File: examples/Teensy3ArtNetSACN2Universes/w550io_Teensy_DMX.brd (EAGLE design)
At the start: 98.7 x 64.8 mm, 33 parts, among them IC1 MAX481CPA, IC2 MAX481CPA

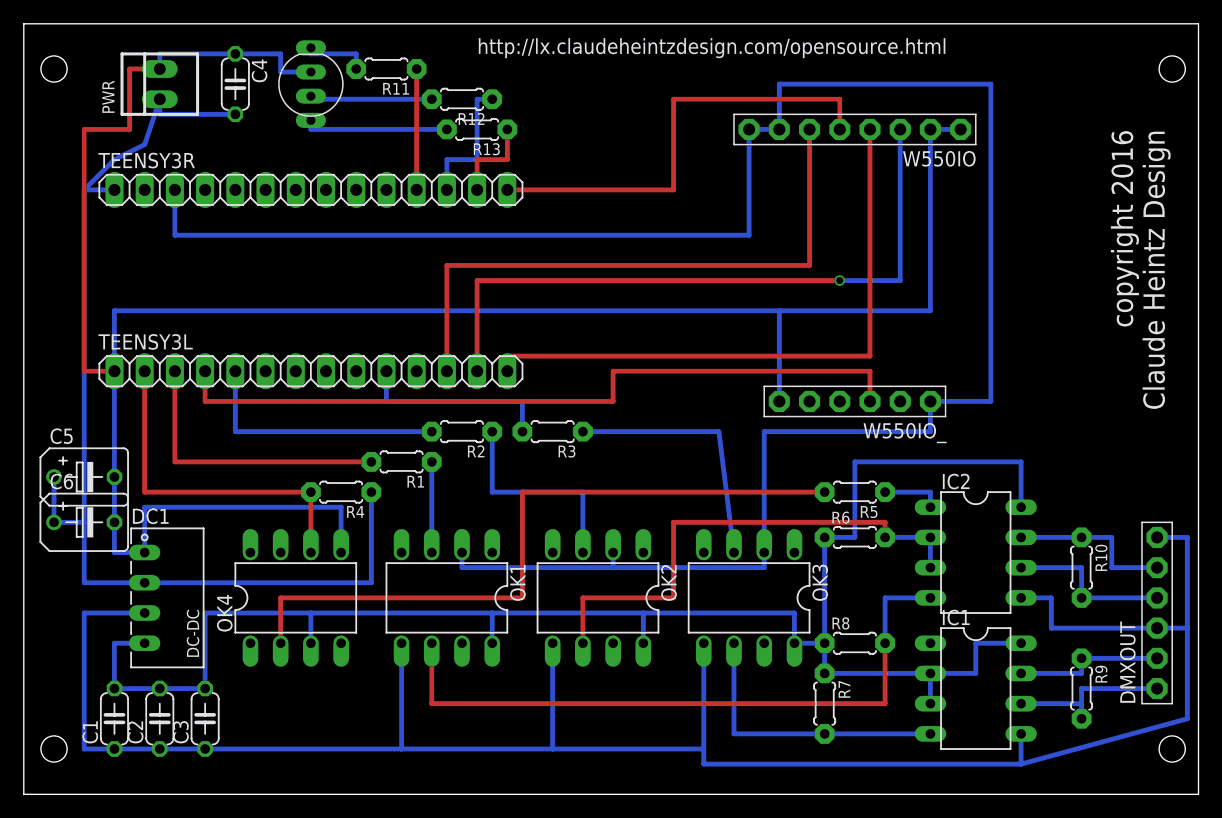
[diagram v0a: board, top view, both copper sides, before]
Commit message: Change Board to output only
Bi-directional design power is unstable.  Previous design is functional
by not populating input and direction optocouplers.
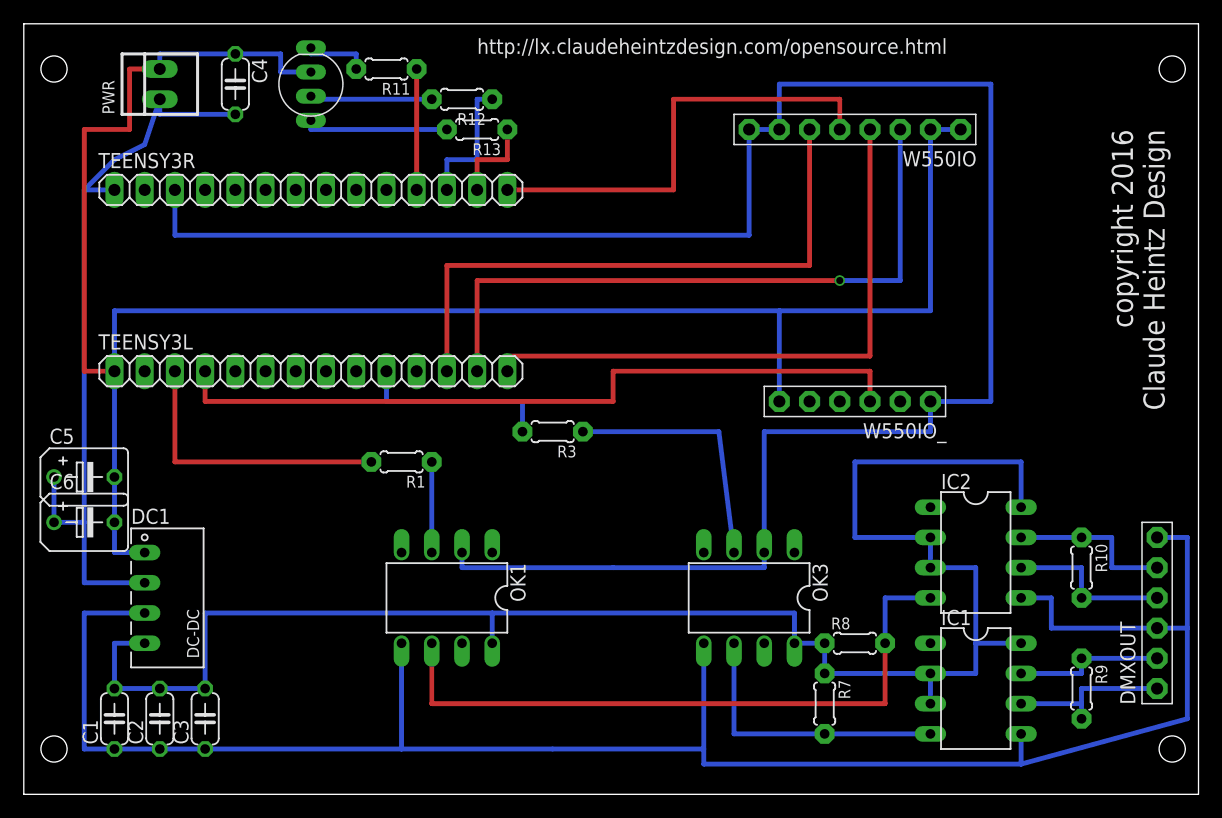
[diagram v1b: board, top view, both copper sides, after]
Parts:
- removed OK2, OK4: 6N137, optocoupler:DIL08
- removed R2: 330, adafruit:0204/5
- removed R4, R6: 10k, adafruit:0204/5
- removed R5: 470, adafruit:0204/5
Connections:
- removed net DX0: R2.2, TEENSY3L.5
- removed net N$1: OK4.2, R5.2
- removed net N$12: IC2.1, R5.1
- removed net N$13: IC2.2, IC2.3, OK2.6, R6.2
- removed net N$6: OK2.3, R2.1
- removed net RX0: OK4.6, R4.2, TEENSY3L.2
- net 3.3V: no longer OK2.2
- net 5VIN: no longer R4.1
- net GND: no longer OK2.5
- net TGND: no longer OK4.5
- net VCC: now also IC2.2, IC2.3; no longer OK2.8, OK4.3, R6.1
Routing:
- net N$1: track 58.4 -> 0.00 mm
- net N$13: track 43.2 -> 0.00 mm
- net RX0: track 29.2 -> 0.00 mm
- net 5VIN: track 91.7 -> 65.1 mm
- net TGND: track 190.8 -> 166.6 mm
- net DX0: track 21.6 -> 0.00 mm
- net N$6: track 17.8 -> 0.00 mm
- net GND: track 174.5 -> 165.6 mm
- net N$12: track 5.08 -> 0.00 mm
- net VCC: track 142.2 -> 144.8 mm
- net 3.3V: track 172.7 -> 171.5 mm

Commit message: Changed 10k Resistors to 1k
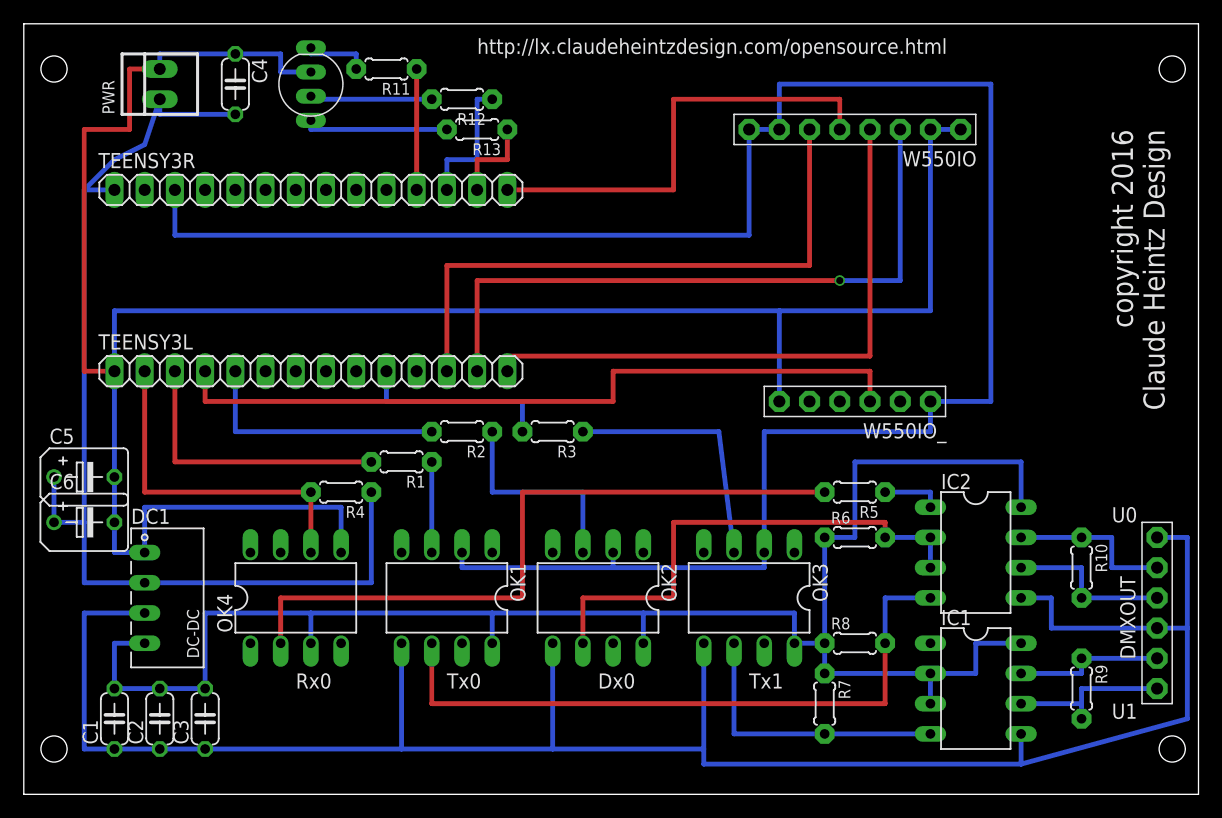
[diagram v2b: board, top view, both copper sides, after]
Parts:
- added OK2, OK4: 6N137, optocoupler:DIL08
- added R2: 330Ω, adafruit:0204/5
- added R4, R6: 1k, adafruit:0204/5
- added R5: 470Ω, adafruit:0204/5
- R1, R11, R12, R13, R3: value 330 -> 330Ω
- R7, R8: value 10k -> 1k
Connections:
- new net DX0: R2.2, TEENSY3L.5
- new net N$1: OK4.2, R5.2
- new net N$12: IC2.1, R5.1
- new net N$13: IC2.2, IC2.3, OK2.6, R6.2
- new net N$6: OK2.3, R2.1
- new net RX0: OK4.6, R4.2, TEENSY3L.2
- net 3.3V: now also OK2.2
- net 5VIN: now also R4.1
- net GND: now also OK2.5
- net TGND: now also OK4.5
- net VCC: now also OK2.8, OK4.3, R6.1; no longer IC2.2, IC2.3
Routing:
- net N$1: track 0.00 -> 58.4 mm
- net N$13: track 0.00 -> 43.2 mm
- net RX0: track 0.00 -> 29.2 mm
- net 5VIN: track 65.1 -> 91.7 mm
- net TGND: track 166.6 -> 190.8 mm
- net DX0: track 0.00 -> 21.6 mm
- net N$6: track 0.00 -> 17.8 mm
- net GND: track 165.6 -> 174.5 mm
- net N$12: track 0.00 -> 5.08 mm
- net VCC: track 144.8 -> 142.2 mm
- net 3.3V: track 171.5 -> 172.7 mm
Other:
- board text added: "Dx0"
- board text added: "Rx0"
- board text added: "Tx0"
- board text added: "Tx1"
- board text added: "U0"
- board text added: "U1"

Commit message: Changed resistors to 3.3k
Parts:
- R4: value 1k -> 10k
- R6, R7, R8: value 1k -> 3.3k
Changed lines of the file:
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@@
 <element name="R2" library="adafruit" package="0204/5" value="330Ω" x="34.29" y="29.21" rot="R180"/>
 <element name="R3" library="adafruit" package="0204/5" value="330Ω" x="41.91" y="29.21" rot="R180"/>
-<element name="R4" library="adafruit" package="0204/5" value="1k" x="24.13" y="24.13" rot="R180"/>
+<element name="R4" library="adafruit" package="0204/5" value="10k" x="24.13" y="24.13" rot="R180"/>
 <element name="IC1" library="maxim" package="DIL08" value="MAX481CPA" x="77.47" y="7.62" rot="R270">
 <attribute name="OC_FARNELL" value="unknown" x="77.47" y="7.62" size="1.778" layer="27" rot="R270" display="off"/>
@@
 </element>
 <element name="R5" library="adafruit" package="0204/5" value="470Ω" x="67.31" y="24.13" rot="R180"/>
-<element name="R6" library="adafruit" package="0204/5" value="1k" x="67.31" y="20.32"/>
-<element name="R7" library="adafruit" package="0204/5" value="1k" x="64.77" y="6.35" rot="R270"/>
-<element name="R8" library="adafruit" package="0204/5" value="1k" x="67.31" y="11.43"/>
+<element name="R6" library="adafruit" package="0204/5" value="3.3k" x="67.31" y="20.32"/>
+<element name="R7" library="adafruit" package="0204/5" value="3.3k" x="64.77" y="6.35" rot="R270"/>
+<element name="R8" library="adafruit" package="0204/5" value="3.3k" x="67.31" y="11.43"/>
 <element name="R9" library="adafruit" package="0204/5" value="120" x="86.36" y="7.62" rot="R270"/>
 <element name="R10" library="adafruit" package="0204/5" value="120" x="86.36" y="17.78" rot="R270"/>

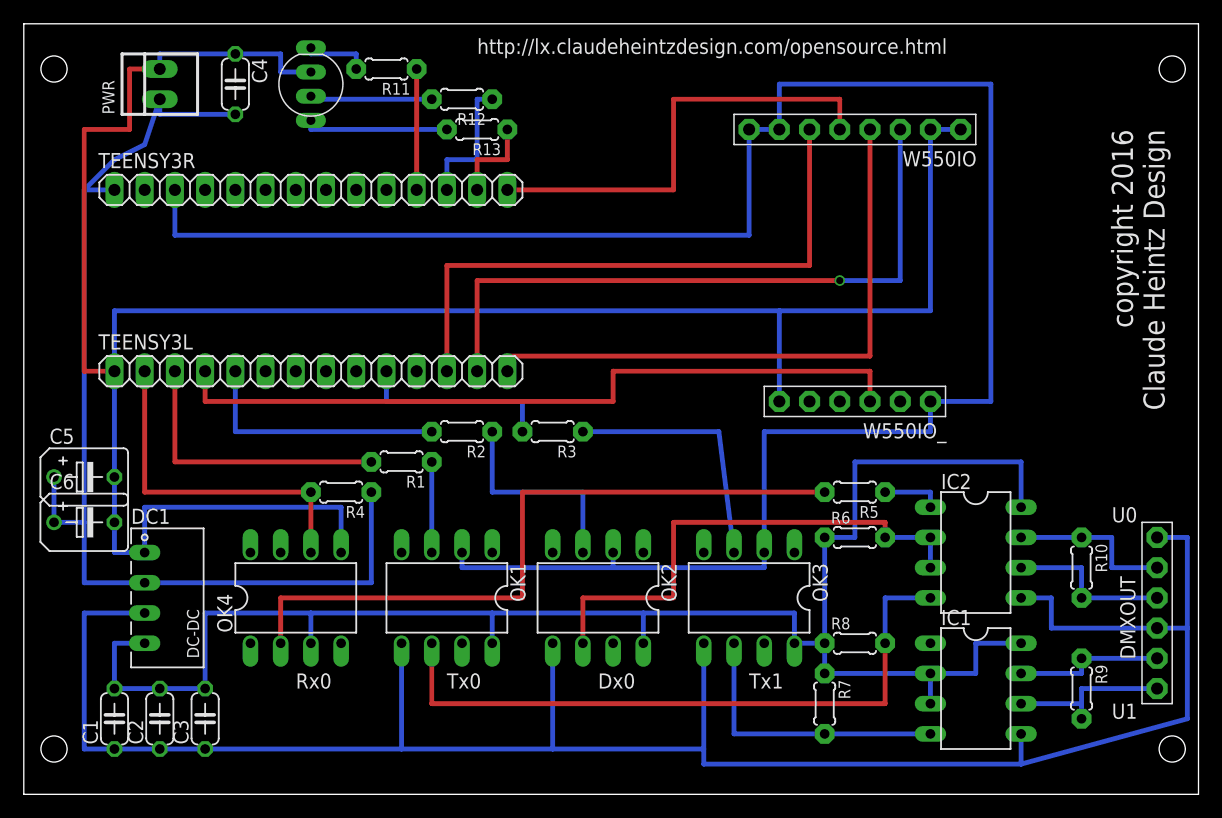
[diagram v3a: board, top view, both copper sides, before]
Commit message: Fix DMX input / example schematic
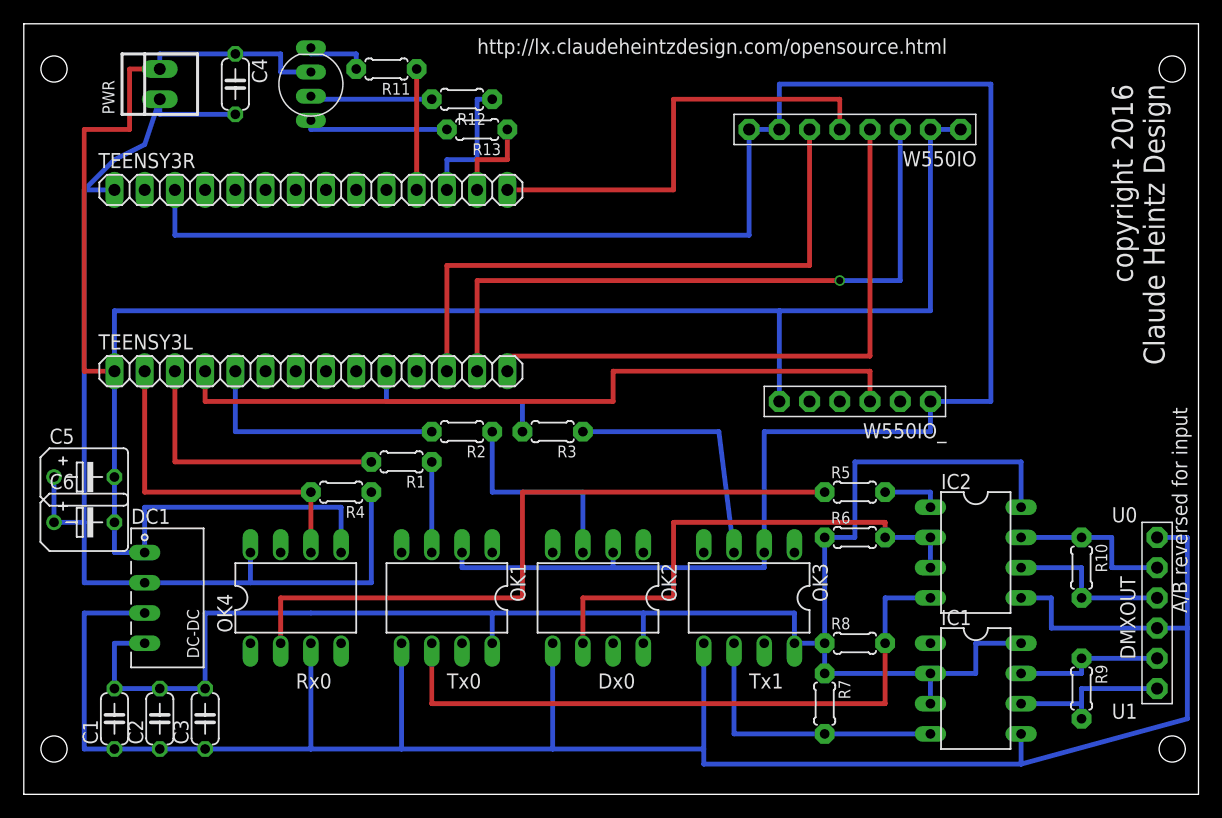
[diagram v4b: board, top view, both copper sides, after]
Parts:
- turned R5 to 0 degrees
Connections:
- net 5VIN: now also OK4.8
- net GND: now also OK4.3
- net N$1: now also R5.1; no longer R5.2
- net N$12: now also R5.2; no longer R5.1
- net VCC: no longer OK4.3
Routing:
- net GND: track 174.5 -> 183.4 mm
- net VCC: track 142.2 -> 139.7 mm
- net 5VIN: track 91.7 -> 94.3 mm
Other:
- board text added: "A/B reversed for input"
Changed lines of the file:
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@@
 <hole x="0" y="59.69" drill="2.2"/>
 <text x="35.56" y="60.96" size="1.27" layer="25" font="vector">http://lx.claudeheintzdesign.com/opensource.html</text>
-<text x="88.9" y="54.61" size="1.778" layer="25" font="vector" rot="R270">copyright 2016
+<text x="88.9" y="58.42" size="1.778" layer="25" font="vector" rot="R270">copyright 2016
 Claude Heintz Design</text>
 <text x="33.02" y="7.62" size="1.27" layer="25">Tx0</text>
@@
 <text x="88.9" y="21.59" size="1.27" layer="25">U0</text>
 <text x="88.9" y="5.08" size="1.27" layer="25">U1</text>
+<text x="95.25" y="13.97" size="1.27" layer="25" rot="R90">A/B reversed for input</text>
 </plain>
 <attributes>
@@
 <attribute name="VALUE" x="90.805" y="7.62" size="1.27" layer="27" rot="R90"/>
 </element>
-<element name="R5" library="adafruit" package="0204/5" value="470Ω" x="67.31" y="24.13" rot="R180"/>
+<element name="R5" library="adafruit" package="0204/5" value="470Ω" x="67.31" y="24.13"/>
 <element name="R6" library="adafruit" package="0204/5" value="3.3k" x="67.31" y="20.32"/>
 <element name="R7" library="adafruit" package="0204/5" value="3.3k" x="64.77" y="6.35" rot="R270"/>
@@
 <contactref element="C5" pad="+"/>
 <contactref element="C6" pad="+"/>
-<wire x1="7.62" y1="16.51" x2="26.67" y2="16.51" width="0.4064" layer="16"/>
+<wire x1="7.62" y1="16.51" x2="16.51" y2="16.51" width="0" layer="19" extent="1-16"/>
+<wire x1="7.62" y1="16.51" x2="16.51" y2="16.51" width="0.4064" layer="16"/>
+<wire x1="16.51" y1="16.51" x2="26.67" y2="16.51" width="0.4064" layer="16"/>
 <wire x1="26.67" y1="16.51" x2="26.67" y2="24.13" width="0.4064" layer="16"/>
 <wire x1="0" y1="25.4" x2="0" y2="21.59" width="0.4064" layer="16"/>
@@
 <wire x1="5.08" y1="52.07" x2="7.62" y2="53.34" width="0.4064" layer="16"/>
 <wire x1="7.62" y1="53.34" x2="8.89" y2="57.15" width="0.4064" layer="16"/>
+<contactref element="OK4" pad="8"/>
+<wire x1="16.51" y1="19.05" x2="16.51" y2="16.51" width="0.4064" layer="16"/>
+<wire x1="16.51" y1="16.51" x2="7.62" y2="16.51" width="0" layer="19" extent="1-16"/>
 </signal>
 <signal name="GND">
@@
 <wire x1="5.08" y1="2.54" x2="8.89" y2="2.54" width="0.4064" layer="16"/>
 <wire x1="8.89" y1="2.54" x2="12.7" y2="2.54" width="0.4064" layer="16"/>
-<wire x1="12.7" y1="2.54" x2="29.21" y2="2.54" width="0.4064" layer="16"/>
+<wire x1="12.7" y1="2.54" x2="21.59" y2="2.54" width="0.4064" layer="16"/>
+<wire x1="21.59" y1="2.54" x2="29.21" y2="2.54" width="0.4064" layer="16"/>
 <wire x1="29.21" y1="2.54" x2="29.21" y2="11.43" width="0.4064" layer="16"/>
 <wire x1="41.91" y1="11.43" x2="41.91" y2="2.54" width="0.4064" layer="16"/>
@@
 <contactref element="OK3" pad="5"/>
 <wire x1="54.61" y1="11.43" x2="54.61" y2="2.54" width="0.4064" layer="16"/>
+<contactref element="OK4" pad="3"/>
+<wire x1="21.59" y1="11.43" x2="21.59" y2="2.54" width="0.4064" layer="16"/>
 </signal>
 <signal name="VCC">
@@
 <contactref element="C2" pad="2"/>
 <contactref element="C3" pad="2"/>
-<contactref element="OK4" pad="3"/>
 <contactref element="OK3" pad="8"/>
 <contactref element="IC1" pad="3"/>
@@
 <wire x1="12.7" y1="7.62" x2="12.7" y2="13.97" width="0.4064" layer="16"/>
 <wire x1="12.7" y1="13.97" x2="21.59" y2="13.97" width="0.4064" layer="16"/>
-<wire x1="21.59" y1="11.43" x2="21.59" y2="13.97" width="0.4064" layer="16"/>
 <wire x1="21.59" y1="13.97" x2="36.83" y2="13.97" width="0.4064" layer="16"/>
 <wire x1="36.83" y1="11.43" x2="36.83" y2="13.97" width="0.4064" layer="16"/>
@@
 <wire x1="57.15" y1="3.81" x2="57.15" y2="11.43" width="0.4064" layer="16"/>
 </signal>
-<signal name="N$1">
-<contactref element="OK4" pad="2"/>
-<contactref element="R5" pad="2"/>
-<wire x1="64.77" y1="24.13" x2="39.37" y2="24.13" width="0.4064" layer="1"/>
-<wire x1="39.37" y1="24.13" x2="39.37" y2="15.24" width="0.4064" layer="1"/>
-<wire x1="39.37" y1="15.24" x2="19.05" y2="15.24" width="0.4064" layer="1"/>
-<wire x1="19.05" y1="15.24" x2="19.05" y2="11.43" width="0.4064" layer="1"/>
-</signal>
 <signal name="N$12">
-<contactref element="R5" pad="1"/>
 <contactref element="IC2" pad="1"/>
 <wire x1="73.66" y1="22.86" x2="73.66" y2="24.13" width="0.4064" layer="16"/>
+<contactref element="R5" pad="2"/>
 <wire x1="73.66" y1="24.13" x2="69.85" y2="24.13" width="0.4064" layer="16"/>
 </signal>
@@
 <wire x1="30.48" y1="49.53" x2="30.48" y2="59.69" width="0.4064" layer="1"/>
 </signal>
+<signal name="N$1">
+<contactref element="R5" pad="1"/>
+<contactref element="OK4" pad="2"/>
+<wire x1="64.77" y1="24.13" x2="39.37" y2="24.13" width="0.4064" layer="1"/>
+<wire x1="39.37" y1="24.13" x2="39.37" y2="15.24" width="0.4064" layer="1"/>
+<wire x1="39.37" y1="15.24" x2="19.05" y2="15.24" width="0.4064" layer="1"/>
+<wire x1="19.05" y1="11.43" x2="19.05" y2="15.24" width="0.4064" layer="1"/>
+</signal>
 </signals>
